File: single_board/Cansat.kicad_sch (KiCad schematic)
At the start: 45 parts, among them J1 XT30_BATTERY, J10 Micro_SD_Card, J11 MAX17048_PLACEHOLDER, J12 BRIDGE_CAST_10, J13 PCB_A_SLOT_10, J14 BRIDGE_CAST_4, J15 PCB_B_SLOT_4, J2 BMP585_PLACEHOLDER, J3 BNO085_PLACEHOLDER, J4 CC1101_MODULE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

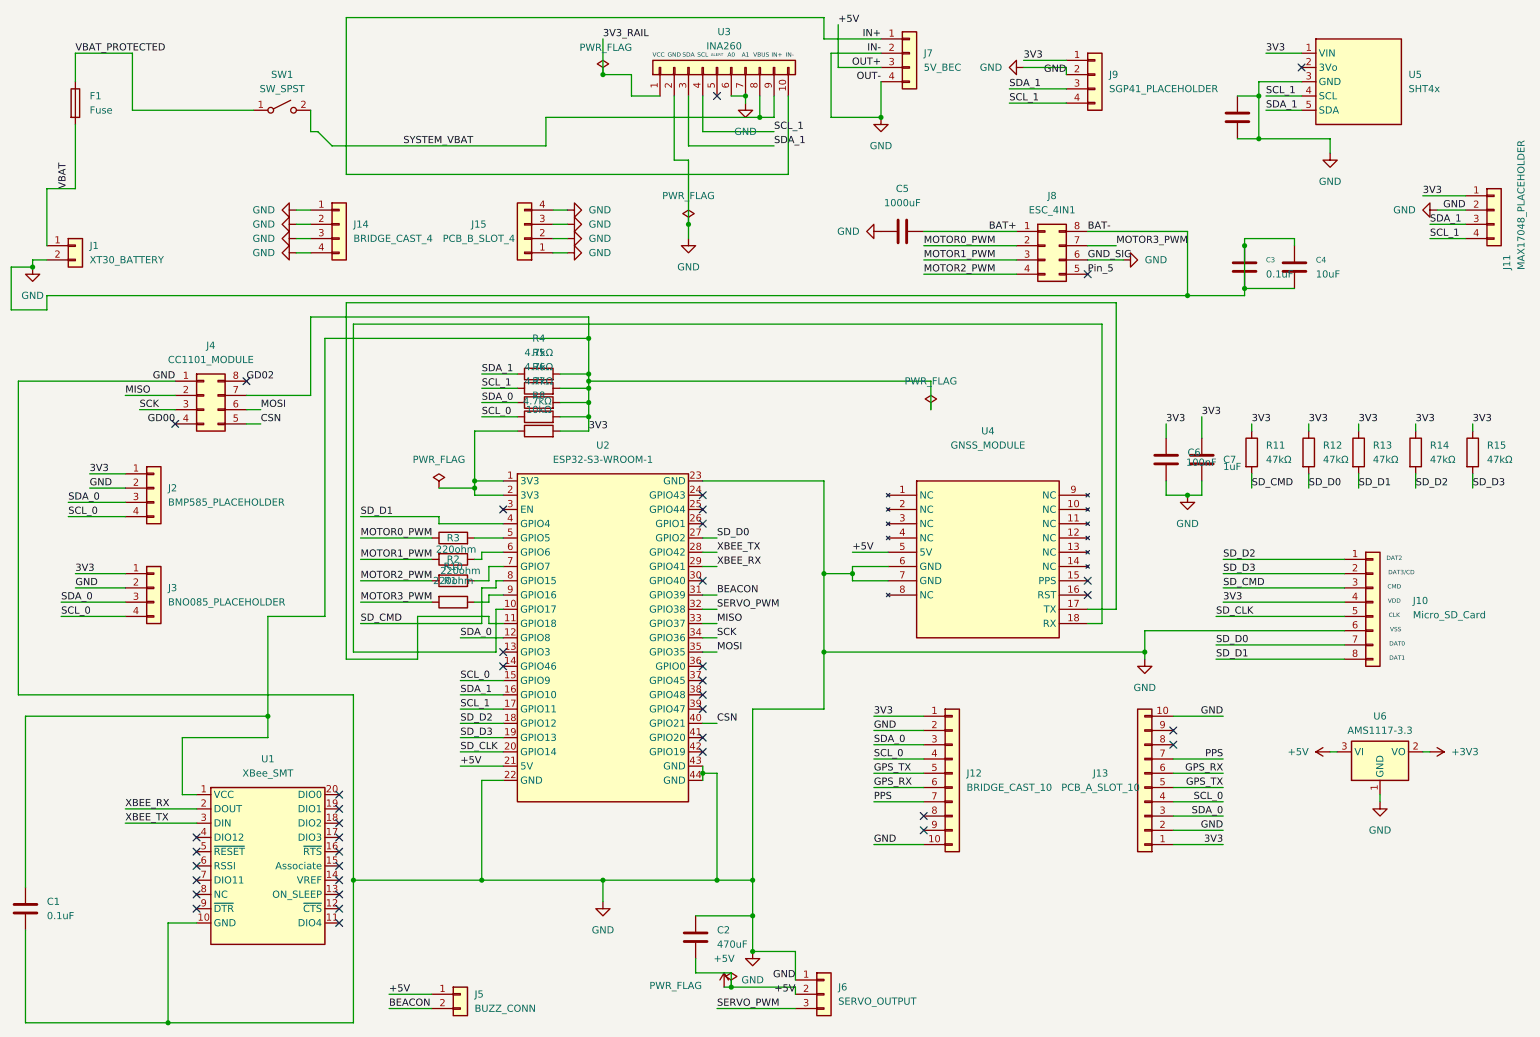
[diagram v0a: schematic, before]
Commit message: Add single_board variant; copy library files; WIP before footprint fix
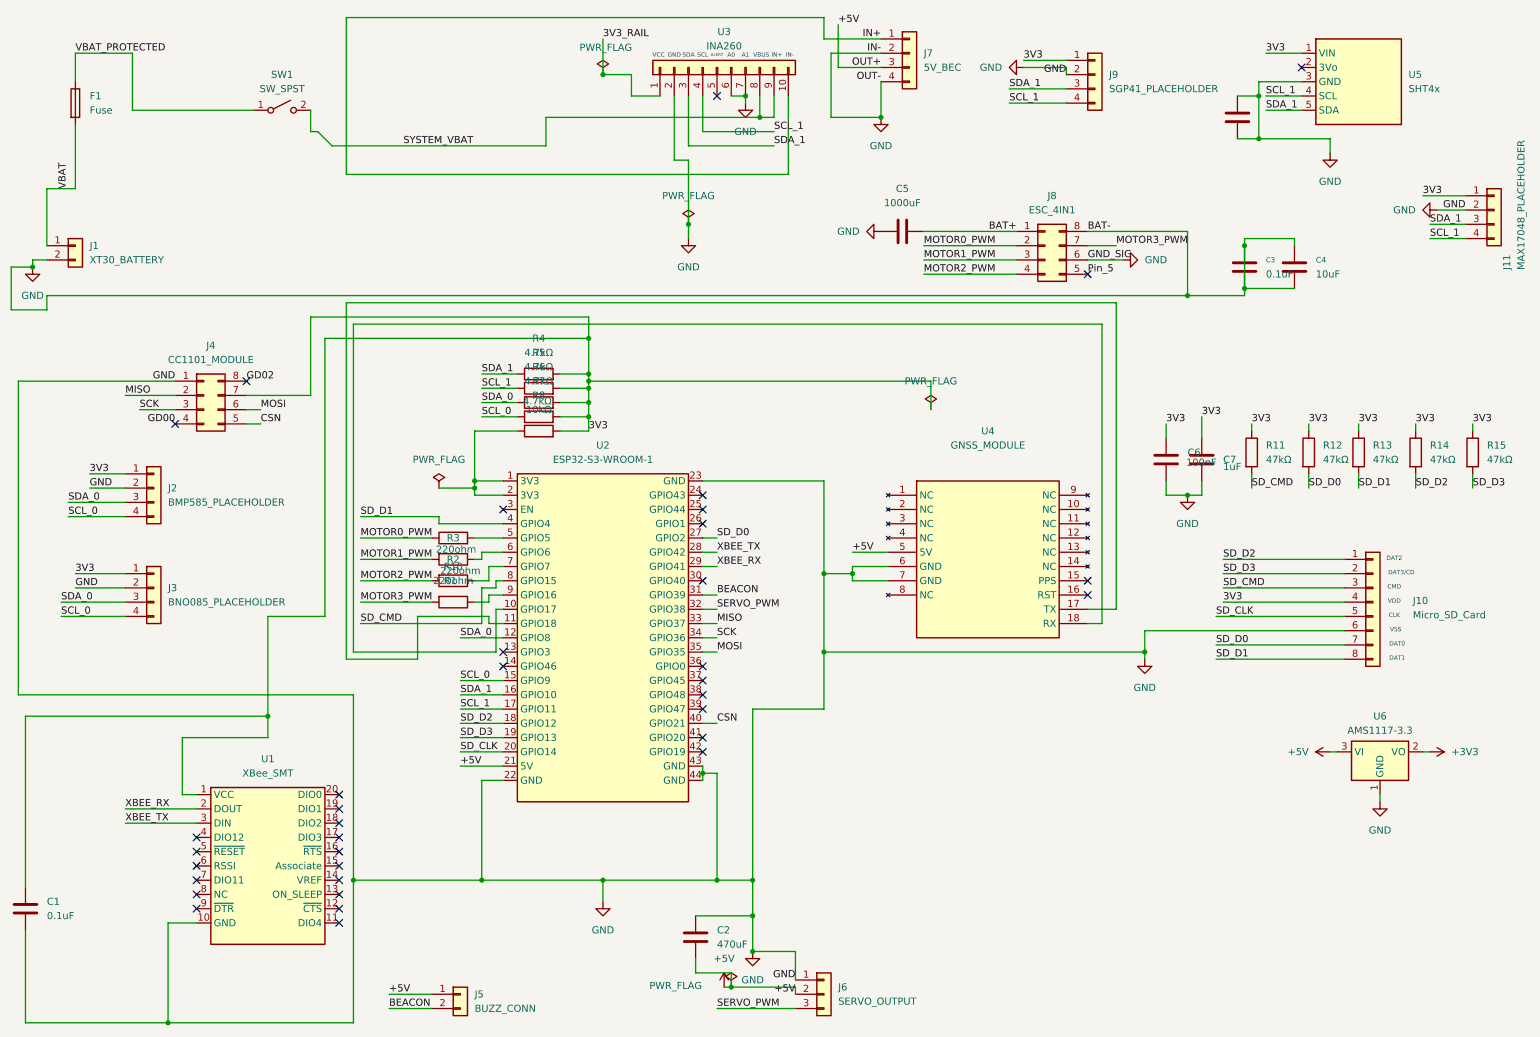
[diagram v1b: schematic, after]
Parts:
- removed J12: BRIDGE_CAST_10, CanSat_Library:BRIDGE_CAST_10, symbol Connector_Generic:Conn_01x10
- removed J13: PCB_A_SLOT_10, CanSat_Library:MAIN_EDGE_SLOT_10, symbol Connector_Generic:Conn_01x10
- removed J14: BRIDGE_CAST_4, CanSat_Library:BRIDGE_CAST_4, symbol Connector_Generic:Conn_01x04
- removed J15: PCB_B_SLOT_4, CanSat_Library:MAIN_EDGE_SLOT_4, symbol Connector_Generic:Conn_01x04
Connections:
- no-connect marks 40 -> 36

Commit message: before patcher
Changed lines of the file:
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@@
-		)
-	)
-	(label "OUT+"
-		(at 167.64 22.86 180)
-		(effects
-			(font
-				(size 1.27 1.27)
-			)
-			(justify right bottom)
 		)
 	)
@@
 		)
 	)
-	(label "GND_SIG"
-		(at 204.47 57.15 0)
-		(effects
-			(font
-				(size 1.27 1.27)
-			)
-			(justify left bottom)
-		)
-	)
 	(label "3V3"
 		(at 115.57 87.63 0)
@@
 		)
 	)
-	(label "IN-"
-		(at 167.64 20.32 180)
-		(effects
-			(font
-				(size 1.27 1.27)
-			)
-			(justify right bottom)
-		)
-	)
 	(label "3V3"
 		(at 262.89 86.36 0)
@@
 		)
 	)
-	(label "BAT-"
-		(at 204.47 52.07 0)
-		(effects
-			(font
-				(size 1.27 1.27)
-			)
-			(justify left bottom)
-		)
-	)
 	(label "3V3"
 		(at 24.13 113.03 0)
@@
 		)
 	)
-	(label "OUT-"
-		(at 167.64 25.4 180)
-		(effects
-			(font
-				(size 1.27 1.27)
-			)
-			(justify right bottom)
-		)
-	)
